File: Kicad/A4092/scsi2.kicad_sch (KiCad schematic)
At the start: 28 parts, among them J3 TO-LED, J4 TO-MB, J8 TO-A3000-LED, J9 TO-A3000-MB, U10 NCR53c710 SCSI Host Controller, Y1 Abracon ACO-50MHz

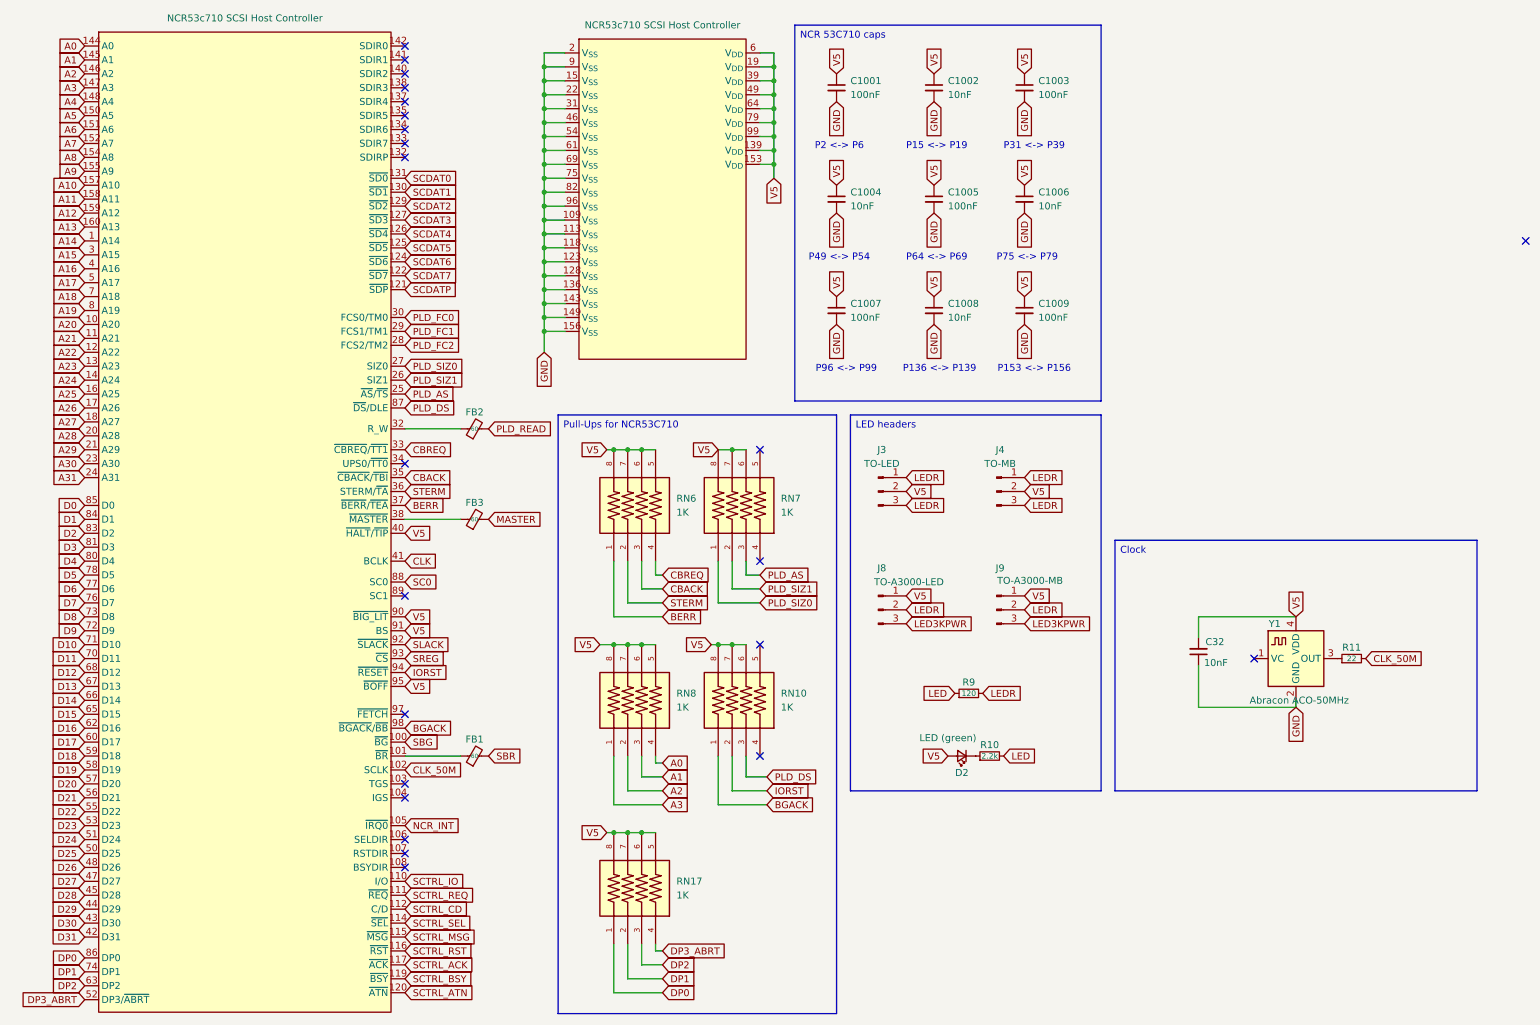
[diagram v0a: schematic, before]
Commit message: A4092 Schematics Revision C
- Power U5 / 74LVC07 from 3.3V rail
- Use ABOEH for 1OEAB on U4 / 74ABT16543
- Add bypass capacitor C501 for U5 / 74LVC07
- Remove EMI filters and capacitors from SCSI lines. They
  are a net negative for signal integrity
- Remove DIP switch circuit as all options are controlled
  by the CPLD / AutoConfig ROM now.
- Remove parallel flash memory, as SPI works reliably and
  is significantly easier to source.
- Remove all ferrite beads from signal lines, as these were
  populated with 0 Ohm resistors in all Proto devices.
- Mark power connector and 12V capacitor as DNP
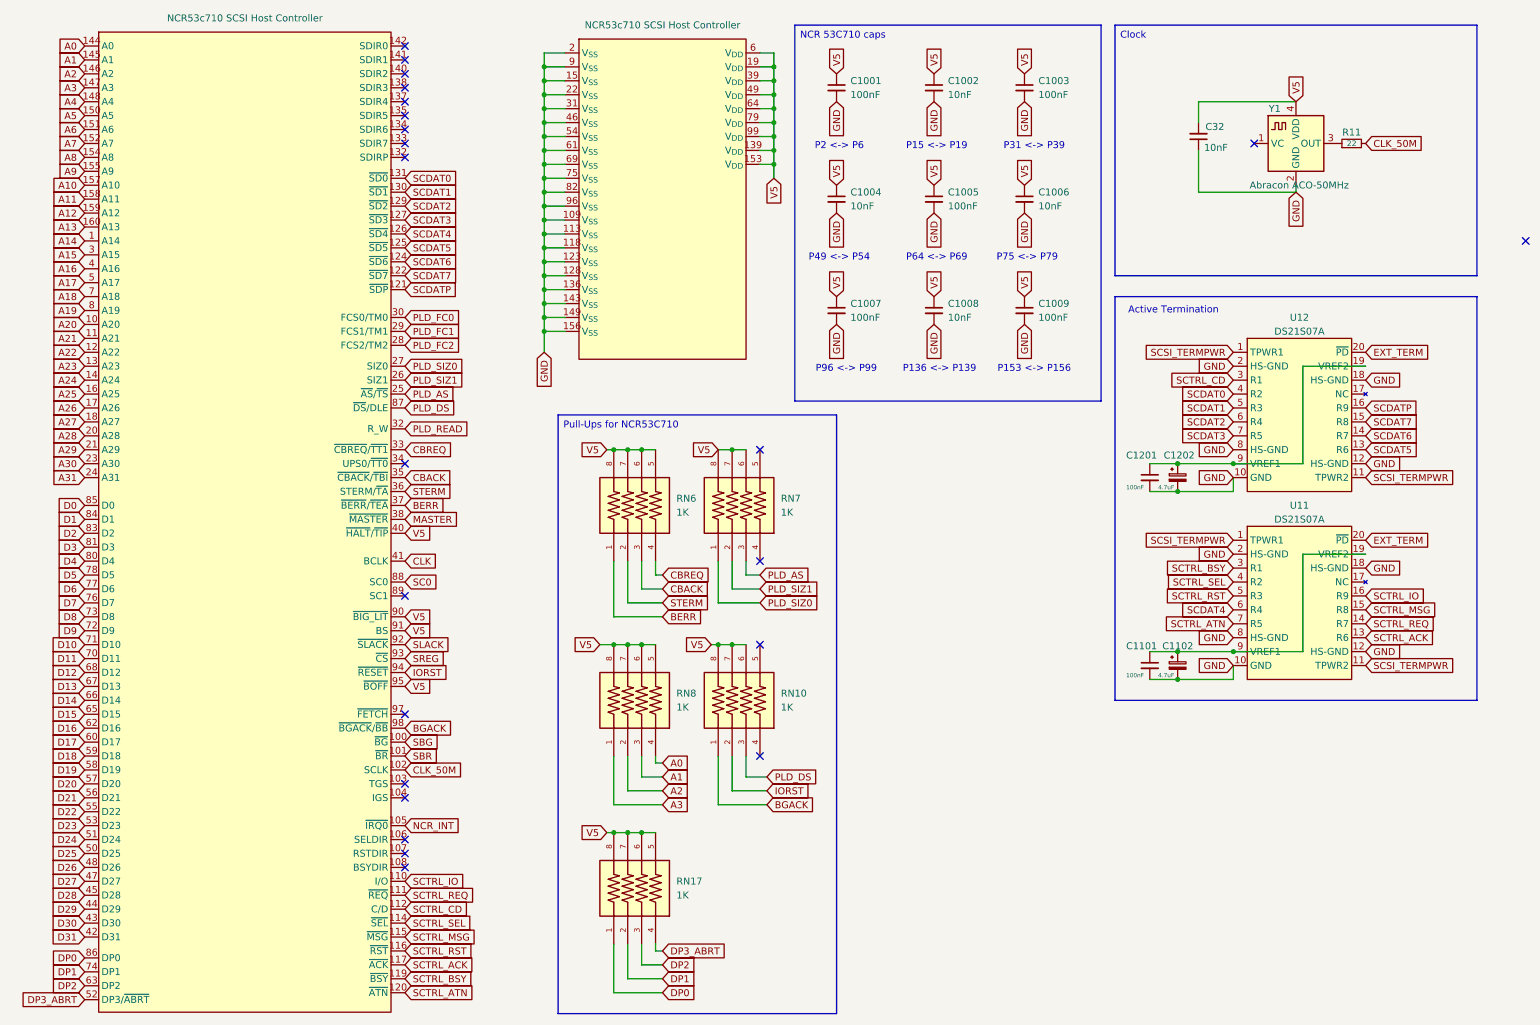
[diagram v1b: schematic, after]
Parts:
- removed D2: LED (green), LED_SMD:LED_0805_2012Metric, symbol Device:LED_Small
- removed FB1, FB2, FB3: 60, Capacitor_SMD:C_0603_1608Metric_Pad1.08x0.95mm_HandSolder, symbol Device:FerriteBead_Small
- removed J3: TO-LED, Connector_PinHeader_2.54mm:PinHeader_1x03_P2.54mm_Vertical, symbol Connector:Conn_01x03_Pin
- removed J4: TO-MB, Connector_PinHeader_2.54mm:PinHeader_1x03_P2.54mm_Vertical, symbol Connector:Conn_01x03_Pin
- removed J8: TO-A3000-LED, Connector_PinHeader_2.54mm:PinHeader_1x03_P2.54mm_Vertical, symbol Connector:Conn_01x03_Pin
- removed J9: TO-A3000-MB, Connector_PinHeader_2.54mm:PinHeader_1x03_P2.54mm_Vertical, symbol Connector:Conn_01x03_Pin
- removed R10: 2.2k, Resistor_SMD:R_0603_1608Metric, symbol Device:R_Small
- removed R9: 120, Resistor_SMD:R_0603_1608Metric, symbol Device:R_Small
- added C1101, C1201: 100nF, Capacitor_SMD:C_0603_1608Metric_Pad1.08x0.95mm_HandSolder, symbol Device:C_Small
- added C1102, C1202: 4.7uF, Capacitor_Tantalum_SMD:CP_EIA-3216-10_Kemet-I_HandSolder, symbol Device:C_Polarized_Small
- added U11, U12: DS21S07A, Package_SO:TSSOP-20_4.4x6.5mm_P0.65mm, symbol ds2107:DS21S07AE
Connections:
- net GND: now also C1101.2, C1102.2, C1201.2, C1202.2, U11.10 (GND), U11.12 (HS-GND), U11.18 (HS-GND), U11.2 (HS-GND), U11.8 (HS-GND), U12.10 (GND), U12.12 (HS-GND), U12.18 (HS-GND), U12.2 (HS-GND), U12.8 (HS-GND)
- net MASTER: now also U10.38 (~{MASTER})
- net PLD_READ: now also U10.32 (R_W)
- net SBR: now also U10.101 (~{BR})
- net SCDAT0: now also U12.4 (R2)
- net SCDAT1: now also U12.5 (R3)
- net SCDAT2: now also U12.6 (R4)
- net SCDAT3: now also U12.7 (R5)
- net SCDAT4: now also U11.6 (R4)
- net SCDAT5: now also U12.13 (R6)
- net SCDAT6: now also U12.14 (R7)
- net SCDAT7: now also U12.15 (R8)
- net SCDATP: now also U12.16 (R9)
- net SCTRL_ACK: now also U11.13 (R6)
- net SCTRL_ATN: now also U11.7 (R5)
- net SCTRL_BSY: now also U11.3 (R1)
- net SCTRL_CD: now also U12.3 (R1)
- net SCTRL_IO: now also U11.16 (R9)
- net SCTRL_MSG: now also U11.15 (R8)
- net SCTRL_REQ: now also U11.14 (R7)
- net SCTRL_RST: now also U11.5 (R3)
- net SCTRL_SEL: now also U11.4 (R2)
- new net: C1101.1, C1102.1, U11.19 (VREF2), U11.9 (VREF1)
- new net: C1201.1, C1202.1, U12.19 (VREF2), U12.9 (VREF1)
- new net EXT_TERM: U11.20 (~{PD}), U12.20 (~{PD})
- new net SCSI_TERMPWR: U11.1 (TPWR1), U11.11 (TPWR2), U12.1 (TPWR1), U12.11 (TPWR2)
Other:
- note added: "Active Termination"
- moved on the sheet: C32, R11, Y1

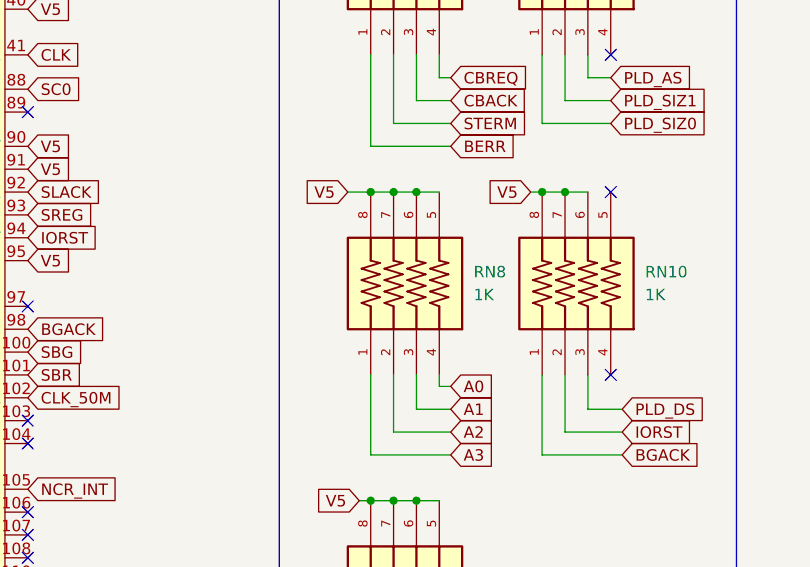
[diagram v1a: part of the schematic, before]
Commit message: Mark unneeded pull-up resistors DNP
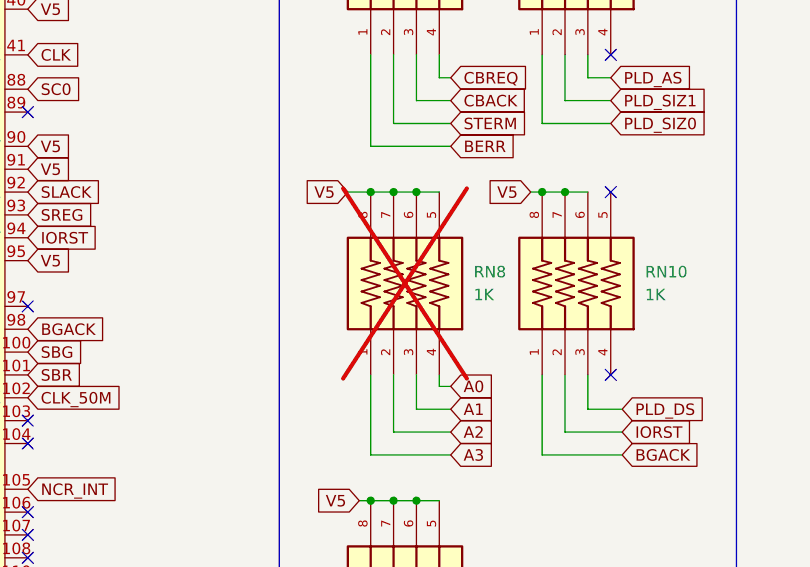
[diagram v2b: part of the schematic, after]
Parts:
- RN8: now not fitted; now left out of the parts list
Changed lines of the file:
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@@
 		(unit 1)
 		(exclude_from_sim no)
-		(in_bom yes)
+		(in_bom no)
 		(on_board yes)
-		(dnp no)
+		(dnp yes)
 		(fields_autoplaced yes)
 		(property "Reference" "RN8"
